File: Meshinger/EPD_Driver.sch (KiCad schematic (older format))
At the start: 17 parts, among them J3 FH34SRJ-24S-0.5SH(99), Q1 MCH3478-TL-W, U3 SS2040FL, U4 SS2040FL, U5 SS2040FL

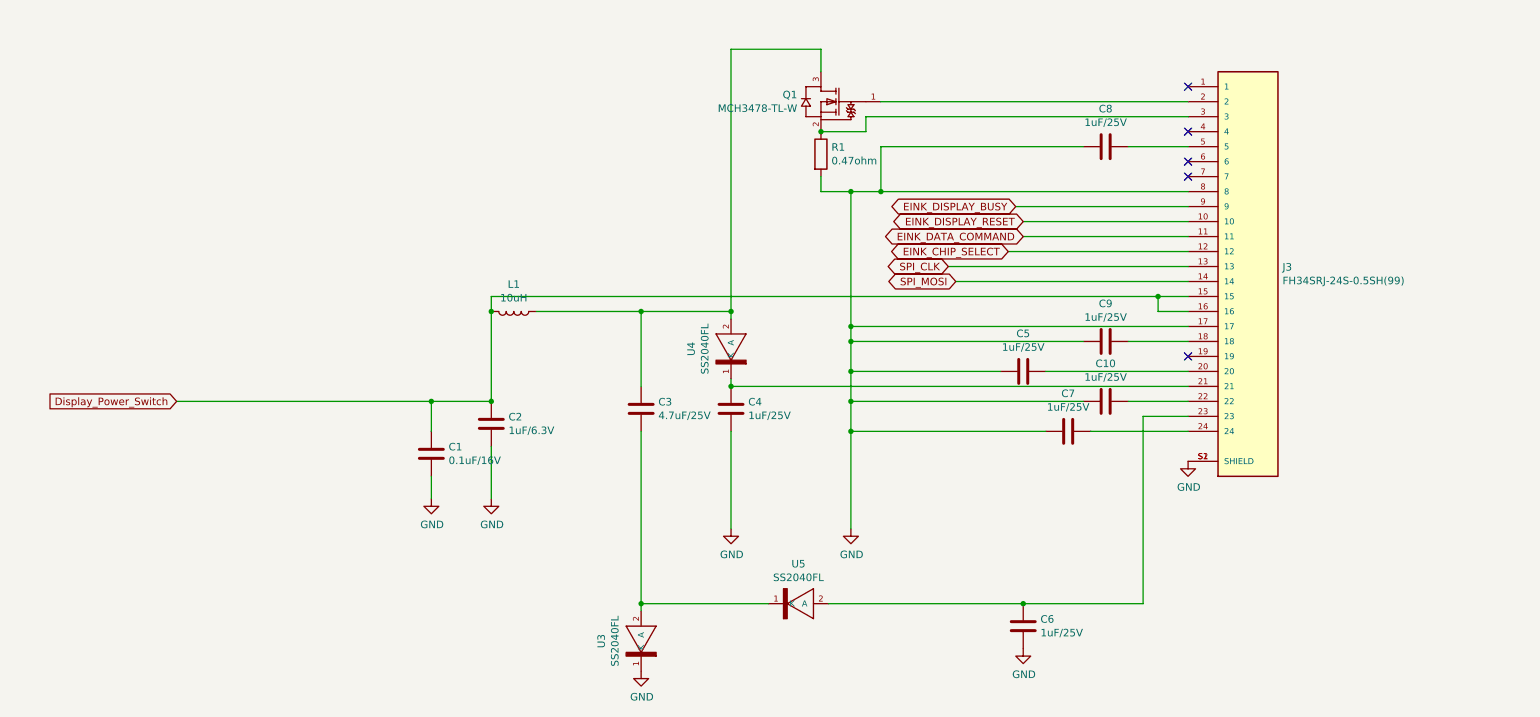
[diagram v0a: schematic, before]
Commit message: Meshinger 1.0 rev B WARNING THE DC PLUG PINS ARE WRONG, SHORTS BATTERY!
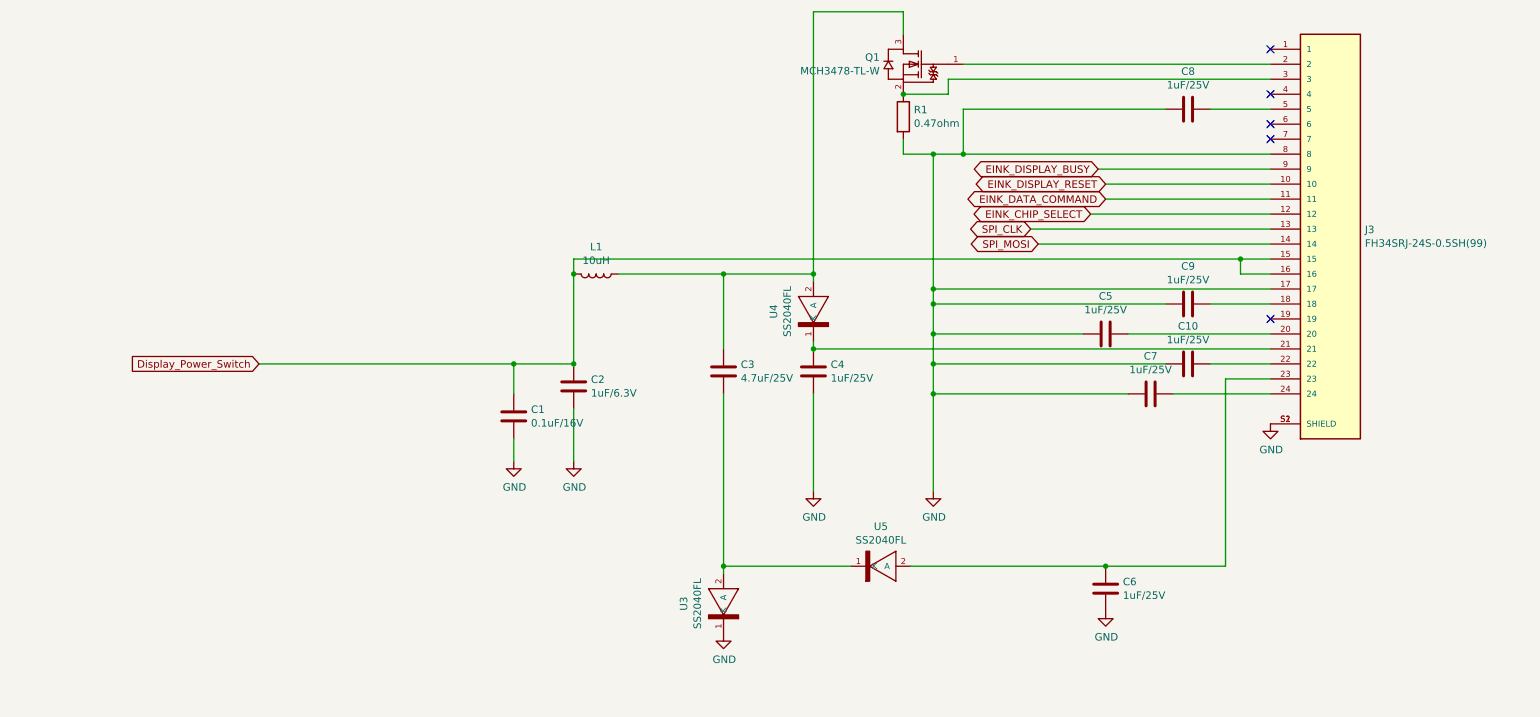
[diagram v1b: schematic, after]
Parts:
- L1: footprint Inductor_SMD:L_0805_2012Metric_Pad1.15x1.40mm_HandSolder -> Inductor_SMD:IND_LQH44PN100MJ0L
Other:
- moved on the sheet: C1, C10, C2, C3, C4, C5, C6, C7, C8, C9, J3, L1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

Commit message: Meshinger 1.0 rev C, Display Power MOSFET heats up while off...
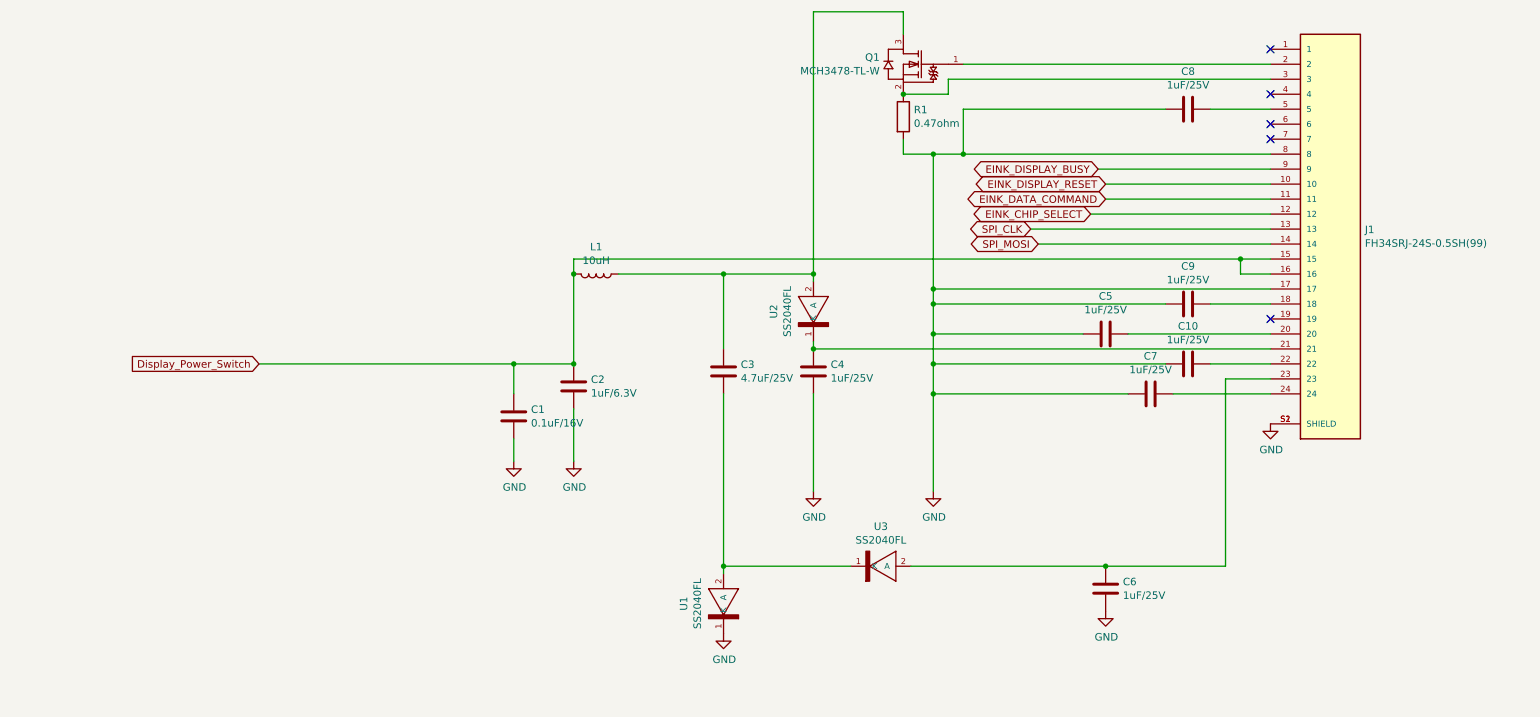
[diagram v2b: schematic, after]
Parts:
- renumbered J3 to J1, U3 to U1, U4 to U2, U5 to U3
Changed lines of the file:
@@
 $EndDescr
 $Comp
-L FH34SRJ-24S:FH34SRJ-24S-0.5SH(99) J3
+L FH34SRJ-24S:FH34SRJ-24S-0.5SH(99) J1
 U 1 1 6039D9C4
 P 9250 2950
-F 0 "J3" H 9480 2946 50  0000 L CNN
+F 0 "J1" H 9480 2946 50  0000 L CNN
 F 1 "FH34SRJ-24S-0.5SH(99)" H 9480 2855 50  0000 L CNN
 F 2 "FH34SRJ-24S:HRS_FH34SRJ-24S-0.5SH(99)" H 9480 2809 50  0001 L CNN
@@
 	8200 4050 8850 4050
 $Comp
-L power:GND #PWR0101
+L power:GND #PWR05
 U 1 1 603BE245
 P 6600 4700
-F 0 "#PWR0101" H 6600 4450 50  0001 C CNN
+F 0 "#PWR05" H 6600 4450 50  0001 C CNN
 F 1 "GND" H 6605 4527 50  0000 C CNN
 F 2 "" H 6600 4700 50  0001 C CNN
@@
 Connection ~ 6600 4050
 $Comp
-L SS2040FL:SS2040FL U4
+L SS2040FL:SS2040FL U2
 U 1 1 603C0F68
 P 5800 3500
-F 0 "U4" H 5800 3765 50  0000 C CNN
+F 0 "U2" H 5800 3765 50  0000 C CNN
 F 1 "SS2040FL" H 5800 3674 50  0000 C CNN
 F 2 "SOD-123FL" H 5800 3500 50  0001 L BNN
@@
 Connection ~ 5800 3750
 $Comp
-L power:GND #PWR0103
+L power:GND #PWR04
 U 1 1 603D71BB
 P 5800 4700
-F 0 "#PWR0103" H 5800 4450 50  0001 C CNN
+F 0 "#PWR04" H 5800 4450 50  0001 C CNN
 F 1 "GND" H 5805 4527 50  0000 C CNN
 F 2 "" H 5800 4700 50  0001 C CNN
@@
 	5200 3250 5800 3250
 $Comp
-L SS2040FL:SS2040FL U3
+L SS2040FL:SS2040FL U1
 U 1 1 603DAD37
 P 5200 5450
-F 0 "U3" H 5200 5715 50  0000 C CNN
+F 0 "U1" H 5200 5715 50  0000 C CNN
 F 1 "SS2040FL" H 5200 5624 50  0000 C CNN
 F 2 "SOD-123FL" H 5200 5450 50  0001 L BNN
@@
 $EndComp
 $Comp
-L SS2040FL:SS2040FL U5
+L SS2040FL:SS2040FL U3
 U 1 1 603DB8DE
 P 6250 5200
-F 0 "U5" H 6250 5465 50  0000 C CNN
+F 0 "U3" H 6250 5465 50  0000 C CNN
 F 1 "SS2040FL" H 6250 5374 50  0000 C CNN
 F 2 "SOD-123FL" H 6250 5200 50  0001 L BNN
@@
 $EndComp
 $Comp
-L power:GND #PWR0104
+L power:GND #PWR03
 U 1 1 603DD981
 P 5200 5650
-F 0 "#PWR0104" H 5200 5400 50  0001 C CNN
+F 0 "#PWR03" H 5200 5400 50  0001 C CNN
 F 1 "GND" H 5205 5477 50  0000 C CNN
 F 2 "" H 5200 5650 50  0001 C CNN
@@
 $EndComp
 $Comp
-L power:GND #PWR0105
+L power:GND #PWR06
 U 1 1 603E05E9
 P 7750 5500
-F 0 "#PWR0105" H 7750 5250 50  0001 C CNN
+F 0 "#PWR06" H 7750 5250 50  0001 C CNN
 F 1 "GND" H 7755 5327 50  0000 C CNN
 F 2 "" H 7750 5500 50  0001 C CNN
@@
 $EndComp
 $Comp
-L power:GND #PWR0106
+L power:GND #PWR02
 U 1 1 603E812B
 P 4200 4500
-F 0 "#PWR0106" H 4200 4250 50  0001 C CNN
+F 0 "#PWR02" H 4200 4250 50  0001 C CNN
 F 1 "GND" H 4205 4327 50  0000 C CNN
 F 2 "" H 4200 4500 50  0001 C CNN
@@
 $EndComp
 $Comp
-L power:GND #PWR0107
+L power:GND #PWR01
 U 1 1 603EAF1F
 P 3800 4500
-F 0 "#PWR0107" H 3800 4250 50  0001 C CNN
+F 0 "#PWR01" H 3800 4250 50  0001 C CNN
 F 1 "GND" H 3805 4327 50  0000 C CNN
 F 2 "" H 3800 4500 50  0001 C CNN
@@
 Connection ~ 3800 3850
 $Comp
-L power:GND #PWR0108
+L power:GND #PWR07
 U 1 1 603F4497
 P 8850 4250
-F 0 "#PWR0108" H 8850 4000 50  0001 C CNN
+F 0 "#PWR07" H 8850 4000 50  0001 C CNN
 F 1 "GND" H 8855 4077 50  0000 C CNN
 F 2 "" H 8850 4250 50  0001 C CNN
